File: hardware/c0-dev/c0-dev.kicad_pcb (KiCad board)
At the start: 2 copper layers, 160 x 68 mm, 456 parts, among them J101 2913730000, J102 2913730000, J103 2913730000, J104 2913730000, J105 2913730000, J106 2913730000, J107 2913730000, J108 2913730000, J109 2913730000, J110 2913730000, J111 2913730000, J112 2913730000, J201 RJ45_LED_Shielded, J401 TAG_CONNECT, J402 PinHeader_2.54mm, Q1001 BSS138P, Q1002 BSS138P, Q1003 BSS138P, Q1004 BSS138P, Q1005 BSS138P, Q1006 BSS138P, Q1007 BSS138P, Q1008 BSS138P, Q1009 BSS138P, Q701 BSS138P, Q702 BSS138P, U1001 TCA9555PWR, U1002 TPS4H000A-Q1, U1003 TPS4H000A-Q1, U1101 LM5160A, U1102 LM317L, U1301 TPS4H000A-Q1, U201 LAN8720A, U301 AP63203WU, U302 TPS2378, U303 TPS54360DDA, U304 TLP175A, U401 TCA9555PWR, U402 W25Q128JVP, U403 RP2350A, U404 TPS3820-33DBV, U501 B0505S-1WR3, U502 ISO1540, U503 ISO1540, U504 TMP117xxDRV, U505 AMS1117-3.3, U506 TMP117xxDRV, U507 ADS1015IDGS, U508 ADS1015IDGS, U601 ADS1015IDGS, U602 ADS1015IDGS, U603 ADS1015IDGS, U604 ADS1015IDGS, U701 B0505S-1WR3, U702 ISO6741, U703 ISO6741, U704 ADS1220xPW, U705 ADS1220xPW, U801 B0505S-1WR3, U802 ISO1044BD, U803 TLP175A, U901 ISO1212, U902 ISO1212, U903 ISO1212, U904 ISO1212, Y401 ABM8-272-T3 (12Mhz)

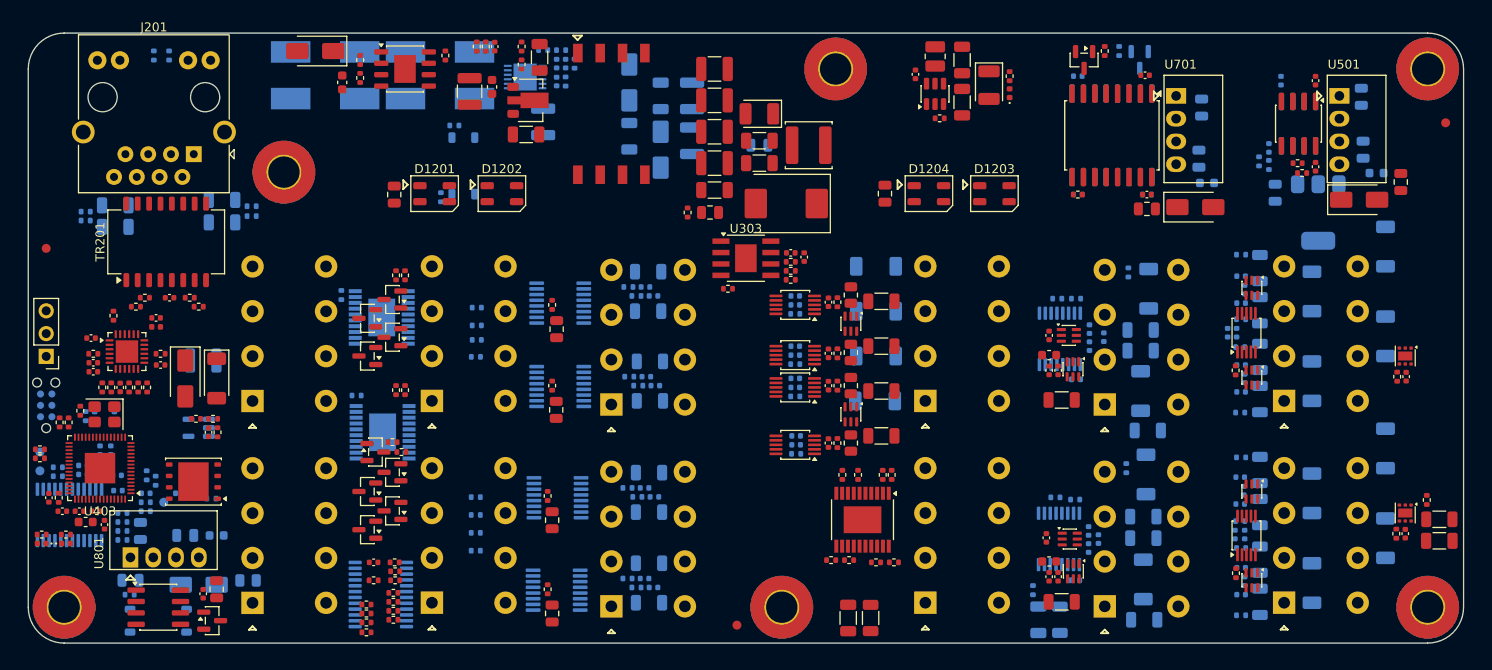
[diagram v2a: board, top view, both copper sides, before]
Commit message: improved isolation
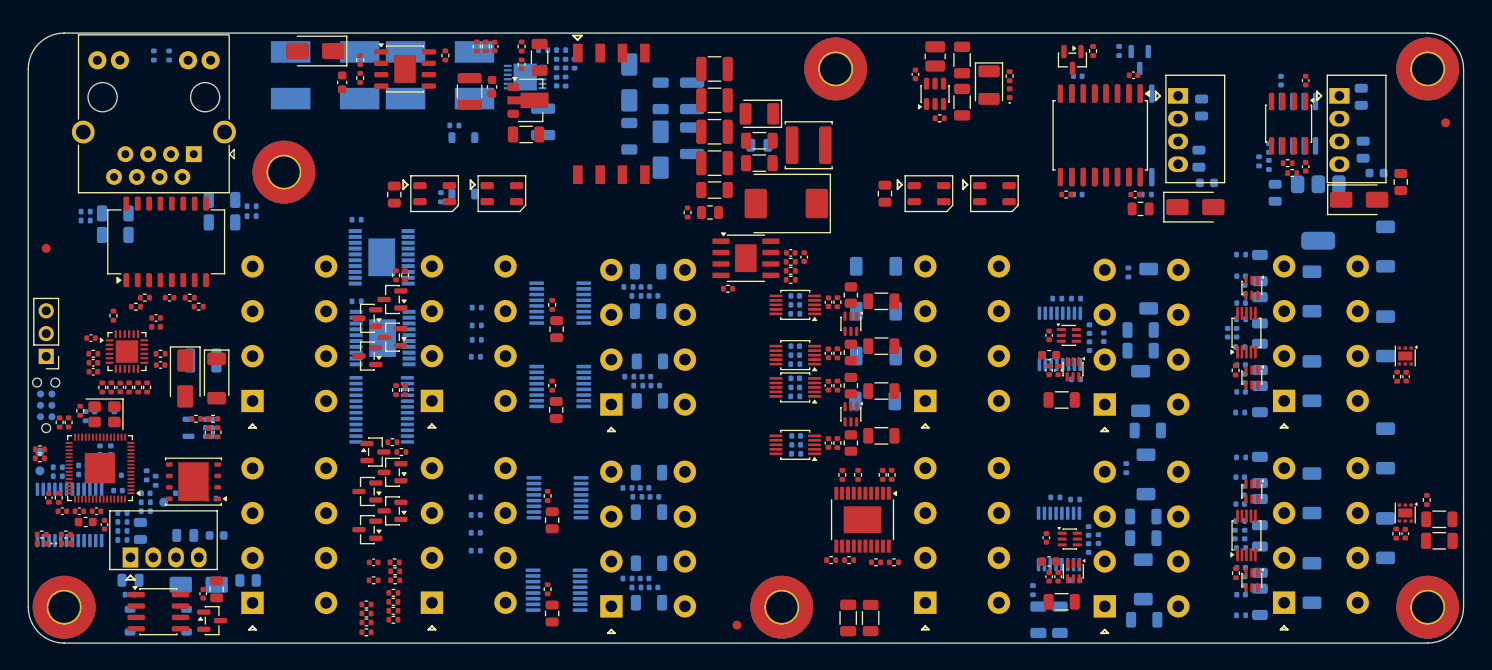
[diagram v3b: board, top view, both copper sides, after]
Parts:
- moved U1001 20.6 mm to (99.4, 104.0)
- moved R1010 10.5 mm to (96.6, 91.9)
- moved U1003 10.5 mm to (99.5, 96.0)
- moved R1007 8.57 mm to (96.6, 82.8), turned to 180 degrees
- moved U1002 6.70 mm to (99.4, 87.0)
- moved C702 1.30 mm to (183.2, 66.7)
- moved R701 1.30 mm to (178.7, 64.0)
- moved R704 1.30 mm to (175.7, 80.0)
- moved U702 1.30 mm to (179.5, 73.4)
- moved C705 1.30 mm to (183.4, 80.0)
- moved Q701 1.30 mm to (176.4, 65.0)
- moved C503 1.10 mm to (202.4, 67.3)
- moved C507 1.10 mm to (202.4, 76.9)
- moved R502 1.10 mm to (200.9, 77.6)
- moved R503 1.10 mm to (200.4, 76.5)
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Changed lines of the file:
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@@
 		(capping no)
 		(filling no)
-		(zone_defaults)
 		(pcbplotparams
 			(layerselection 0x00000000_00000000_55555555_5755f5ff)
@@
 	(footprint "Capacitor_SMD:C_0402_1005Metric"
 		(layer "F.Cu")
-		(at 203.5 76.9 -90)
+		(at 202.4 76.9 -90)
 		(descr "Capacitor SMD 0402 (1005 Metric), square (rectangular) end terminal, IPC-7351 nominal, (Body size source: IPC-SM-782 page 76, https://www.pcb-3d.com/wordpress/wp-content/uploads/ipc-sm-782a_amendment_1_and_2.pdf)")
 		(tags "capacitor")
@@
 	(footprint "Resistor_SMD:R_0402_1005Metric"
 		(layer "F.Cu")
-		(at 202 77.6)
+		(at 200.9 77.6)
 		(descr "Resistor SMD 0402 (1005 Metric), square (rectangular) end terminal, IPC-7351 nominal, (Body size source: IPC-SM-782 page 72, https://www.pcb-3d.com/wordpress/wp-content/uploads/ipc-sm-782a_amendment_1_and_2.pdf)")
 		(tags "resistor")
@@
 			(at 0 -7.35 90)
 			(layer "F.SilkS")
+			(hide yes)
 			(effects
 				(font
@@
 	(footprint "Resistor_SMD:R_0402_1005Metric"
 		(layer "F.Cu")
-		(at 180 64 90)
+		(at 178.7 64 90)
 		(descr "Resistor SMD 0402 (1005 Metric), square (rectangular) end terminal, IPC-7351 nominal, (Body size source: IPC-SM-782 page 72, https://www.pcb-3d.com/wordpress/wp-content/uploads/ipc-sm-782a_amendment_1_and_2.pdf)")
 		(tags "resistor")
@@
 			(at 0 -4.8 180)
 			(layer "F.SilkS")
+			(hide yes)
 			(effects
 				(font
@@
 	(footprint "conduit:Converter_DCDC_EVISUN_BXXXXS-1WR3"
 		(layer "F.Cu")
-		(at 187.9575 69)
+		(at 188.175 69)
 		(tags "evisun dc-dc transformer")
 		(property "Reference" "U701"
 			(at 0.5 -3.5 180)
 			(layer "F.SilkS")
+			(hide yes)
 			(effects
 				(font
@@
 			)
 			(layer "F.SilkS")
-			(net "")
 		)
 		(fp_line
@@
 			)
 			(layer "F.SilkS")
-			(net "")
 		)
 		(fp_line
@@
 			)
 			(layer "F.SilkS")
-			(net "")
 		)
 		(fp_line
@@
 			(at 0 -2.75 0)
 			(layer "F.SilkS")
+			(hide yes)
 			(effects
 				(font
@@
 	(footprint "Package_TO_SOT_SMD:SOT-23"
 		(layer "F.Cu")
-		(at 177.7 65 -90)
+		(at 176.4 65 -90)
 		(descr "SOT, 3 Pin (JEDEC TO-236 Var AB https://www.jedec.org/document_search?search_api_views_fulltext=TO-236)")
 		(tags "SOT TO_SOT_SMD")
@@
 	(footprint "Package_SO:SOIC-8_3.9x4.9mm_P1.27mm"
 		(layer "F.Cu")
-		(at 201.6 72.1 -90)
+		(at 200.5 72.1 -90)
 		(descr "SOIC, 8 Pin (JEDEC MS-012AA, https://www.analog.com/media/en/package-pcb-resources/package/pkg_pdf/soic_narrow-r/r_8.pdf)")
 		(tags "SOIC SO")
@@
 	(footprint "Capacitor_SMD:C_0402_1005Metric"
 		(layer "F.Cu")
-		(at 184.5 66.7 180)
+		(at 183.2 66.7 180)
 		(descr "Capacitor SMD 0402 (1005 Metric), square (rectangular) end terminal, IPC-7351 nominal, (Body size source: IPC-SM-782 page 76, https://www.pcb-3d.com/wordpress/wp-content/uploads/ipc-sm-782a_amendment_1_and_2.pdf)")
 		(tags "capacitor")
@@
 			(at 0.5 -3.5 180)
 			(layer "F.SilkS")
+			(hide yes)
 			(effects
 				(font
@@
 			)
 			(layer "F.SilkS")
-			(net "")
 		)
 		(fp_line
@@
 			)
 			(layer "F.SilkS")
-			(net "")
 		)
 		(fp_line
@@
 			)
 			(layer "F.SilkS")
-			(net "")
 		)
 		(fp_line
@@
 	(footprint "Capacitor_SMD:C_0402_1005Metric"
 		(layer "F.Cu")
-		(at 184.7 80 180)
+		(at 183.4 80 180)
 		(descr "Capacitor SMD 0402 (1005 Metric), square (rectangular) end terminal, IPC-7351 nominal, (Body size source: IPC-SM-782 page 76, https://www.pcb-3d.com/wordpress/wp-content/uploads/ipc-sm-782a_amendment_1_and_2.pdf)")
 		(tags "capacitor")
@@
 	(footprint "Capacitor_SMD:C_0805_2012Metric"
 		(layer "F.Cu")
-		(at 184.7 81.6 180)
+		(at 184 81.6 180)
 		(descr "Capacitor SMD 0805 (2012 Metric), square (rectangular) end terminal, IPC-7351 nominal, (Body size source: IPC-SM-782 page 76, https://www.pcb-3d.com/wordpress/wp-content/uploads/ipc-sm-782a_amendment_1_and_2.pdf, https://docs.google.com/spreadsheets/d/1BsfQQcO9C6DZCsRaXUlFlo91Tg2WpOkGARC1WS5S8t0/edit?usp=sharing)")
 		(tags "capacitor")
@@
 	(footprint "Capacitor_SMD:C_0402_1005Metric"
 		(layer "F.Cu")
-		(at 203.5 67.3 90)
+		(at 202.4 67.3 90)
 		(descr "Capacitor SMD 0402 (1005 Metric), square (rectangular) end terminal, IPC-7351 nominal, (Body size source: IPC-SM-782 page 76, https://www.pcb-3d.com/wordpress/wp-content/uploads/ipc-sm-782a_amendment_1_and_2.pdf)")
 		(tags "capacitor")
@@
 			(at 0 -3.3 0)
 			(layer "F.SilkS")
+			(hide yes)
 			(effects
 				(font
@@
 	(footprint "Package_SO:SOIC-8_3.9x4.9mm_P1.27mm"
 		(layer "F.Cu")
-		(at 74.5 126)
+		(at 74.5 126.5)
 		(descr "SOIC, 8 Pin (JEDEC MS-012AA, https://www.analog.com/media/en/package-pcb-resources/package/pkg_pdf/soic_narrow-r/r_8.pdf)")
 		(tags "SOIC SO")
@@
 			(at 0 -2.75 0)
 			(layer "F.SilkS")
+			(hide yes)
 			(effects
 				(font
@@
 	(footprint "Resistor_SMD:R_0402_1005Metric"
 		(layer "F.Cu")
-		(at 201.5 76.5)
+		(at 200.4 76.5)
 		(descr "Resistor SMD 0402 (1005 Metric), square (rectangular) end terminal, IPC-7351 nominal, (Body size source: IPC-SM-782 page 72, https://www.pcb-3d.com/wordpress/wp-content/uploads/ipc-sm-782a_amendment_1_and_2.pdf)")
 		(tags "resistor")
@@
 			(at 0.5 -3.5 270)
 			(layer "F.SilkS")
+			(hide yes)
 			(effects
 				(font
@@
 			)
 			(layer "F.SilkS")
-			(net "")
 		)
 		(fp_line
@@
 			)
 			(layer "F.SilkS")
-			(net "")
 		)
 		(fp_line
@@
 			)
 			(layer "F.SilkS")
-			(net "")
 		)
 		(fp_line
@@
 	(footprint "Resistor_SMD:R_0402_1005Metric"
 		(layer "F.Cu")
-		(at 177 80 180)
+		(at 175.7 80 180)
 		(descr "Resistor SMD 0402 (1005 Metric), square (rectangular) end terminal, IPC-7351 nominal, (Body size source: IPC-SM-782 page 72, https://www.pcb-3d.com/wordpress/wp-content/uploads/ipc-sm-782a_amendment_1_and_2.pdf)")
 		(tags "resistor")
@@
 			(at 4.445 14.15 180)
 			(layer "F.SilkS")
+			(hide yes)
 			(effects
 				(font
@@
 			(at 0 -2.75 0)
 			(layer "F.SilkS")
+			(hide yes)
 			(effects
 				(font
@@
 			(at 0 -2.75 0)
 			(layer "F.SilkS")
+			(hide yes)
 			(effects
 				(font
@@
 	(footprint "Package_SO:SOIC-16W_7.5x10.3mm_P1.27mm"
 		(layer "F.Cu")
-		(at 180.8 73.4 -90)
+		(at 179.5 73.4 -90)
 		(descr "SOIC, 16 Pin (JEDEC MS-013AA, https://www.analog.com/media/en/package-pcb-resources/package/pkg_pdf/soic_wide-rw/rw_16.pdf)")
 		(tags "SOIC SO")
@@
 	(footprint "Package_SO:TSSOP-24_4.4x7.8mm_P0.65mm"
 		(layer "B.Cu")
-		(at 99.303563 124.586283 180)
+		(at 99.4 104 180)
 		(descr "TSSOP, 24 Pin (JEDEC MO-153 variation AD, 1.00mm body thickness, https://www.jedec.org/document_search?search_api_views_fulltext=MO-153)")
 		(tags "TSSOP SO")
@@
 	(footprint "Capacitor_SMD:C_1206_3216Metric"
 		(layer "B.Cu")
-		(at 69.7 81.2 180)
+		(at 69.7 82.1 180)
 		(descr "Capacitor SMD 1206 (3216 Metric), square (rectangular) end terminal, IPC-7351 nominal, (Body size source: IPC-SM-782 page 76, https://www.pcb-3d.com/wordpress/wp-content/uploads/ipc-sm-782a_amendment_1_and_2.pdf)")
 		(tags "capacitor")
@@
 			(at 0 7 90)
 			(layer "B.SilkS")
+			(hide yes)
 			(effects
 				(font
@@
 	(footprint "Capacitor_SMD:C_1206_3216Metric"
 		(layer "B.Cu")
-		(at 69.7 83.6 180)
+		(at 69.7 84.5 180)
 		(descr "Capacitor SMD 1206 (3216 Metric), square (rectangular) end terminal, IPC-7351 nominal, (Body size source: IPC-SM-782 page 76, https://www.pcb-3d.com/wordpress/wp-content/uploads/ipc-sm-782a_amendment_1_and_2.pdf)")
 		(tags "capacitor")
@@
 	(footprint "Resistor_SMD:R_0402_1005Metric"
 		(layer "B.Cu")
-		(at 96.6 102.4 180)
+		(at 96.6 91.9 180)
 		(descr "Resistor SMD 0402 (1005 Metric), square (rectangular) end terminal, IPC-7351 nominal, (Body size source: IPC-SM-782 page 72, https://www.pcb-3d.com/wordpress/wp-content/uploads/ipc-sm-782a_amendment_1_and_2.pdf)")
 		(tags "resistor")
@@
 			(at 0 7 270)
 			(layer "B.SilkS")
+			(hide yes)
 			(effects
 				(font
@@
 	(footprint "Package_SO:ETSSOP-20-1EP_4.4x6.5mm_P0.65mm_EP3x4.2mm"
 		(layer "B.Cu")
-		(at 99.4 93.7)
+		(at 99.4 87)
 		(descr "20-Lead Plastic Thin Shrink Small Outline (ST)-4.4 mm Body with Exposed Pad [eTSSOP] (see Microchip Packaging Specification 00000049BS.pdf)")
 		(tags "SSOP 0.65")
@@
 	(footprint "Resistor_SMD:R_0402_1005Metric"
 		(layer "B.Cu")
-		(at 94.9 91.2 -90)
+		(at 96.6 82.8 180)
 		(descr "Resistor SMD 0402 (1005 Metric), square (rectangular) end terminal, IPC-7351 nominal, (Body size source: IPC-SM-782 page 72, https://www.pcb-3d.com/wordpress/wp-content/uploads/ipc-sm-782a_amendment_1_and_2.pdf)")
 		(tags "resistor")
 		(property "Reference" "R1007"
-			(at 0 1.17 90)
+			(at 0 1.17 0)
 			(layer "B.SilkS")
 			(hide yes)
@@
 		)
 		(property "Value" "4.7k"
-			(at 0 -1.17 90)
+			(at 0 -1.17 0)
 			(layer "B.Fab")
 			(effects
@@
 		)
 		(property "Datasheet" ""
-			(at 0 0 90)
+			(at 0 0 0)
 			(layer "B.Fab")
 			(hide yes)
@@
 		)
 		(property "Description" ""
-			(at 0 0 90)
+			(at 0 0 0)
 			(layer "B.Fab")
 			(hide yes)
@@
 		)
 		(property "KiLib_Generator" "SMD_2terminal_chip_molded"
-			(at 0 0 90)
+			(at 0 0 0)
 			(layer "B.SilkS")
 			(hide yes)
@@
 		)
 		(fp_text user "${REFERENCE}"
-			(at 0 0 90)
+			(at 0 0 0)
 			(layer "B.Fab")
 			(effects
@@
 		)
 		(pad "1" smd roundrect
-			(at -0.51 0 270)
+			(at -0.51 0 180)
 			(size 0.54 0.64)
 			(layers "B.Cu" "B.Mask" "B.Paste")
@@
 		)
 		(pad "2" smd roundrect
-			(at 0.51 0 270)
+			(at 0.51 0 180)
 			(size 0.54 0.64)
 			(layers "B.Cu" "B.Mask" "B.Paste")
@@
 	(footprint "Package_SO:ETSSOP-20-1EP_4.4x6.5mm_P0.65mm_EP3x4.2mm"
 		(layer "B.Cu")
-		(at 99.5 106.5)
+		(at 99.5 96)
 		(descr "20-Lead Plastic Thin Shrink Small Outline (ST)-4.4 mm Body with Exposed Pad [eTSSOP] (see Microchip Packaging Specification 00000049BS.pdf)")
 		(tags "SSOP 0.65")
